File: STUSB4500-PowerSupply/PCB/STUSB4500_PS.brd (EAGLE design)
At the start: 60 x 40 mm, 102 parts, among them J2 FEMALE 2x3, J3 FEMALE 2x3, J4 FEMALE 2x3, SW1 SPST_TACT-EVQQ2

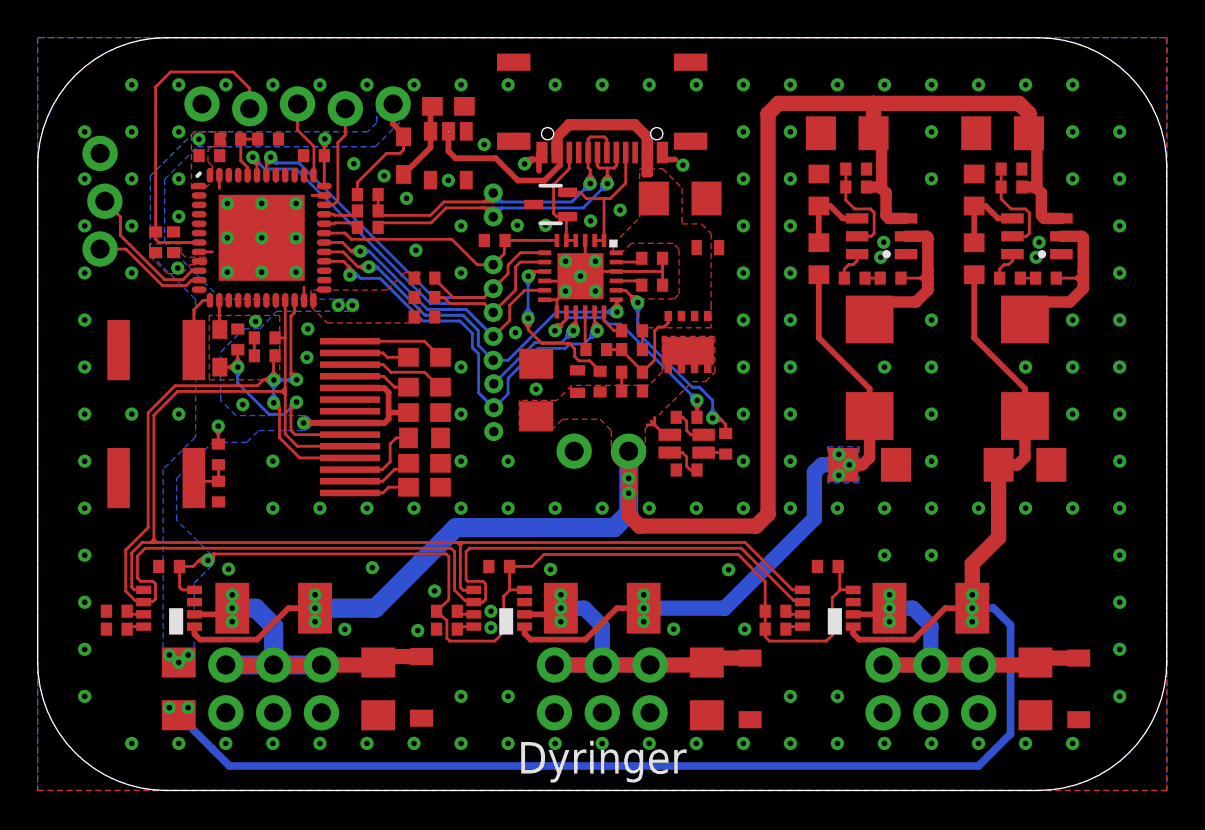
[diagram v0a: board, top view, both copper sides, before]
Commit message: removed some unnecessary elements, added uc controlled dc-dc enable
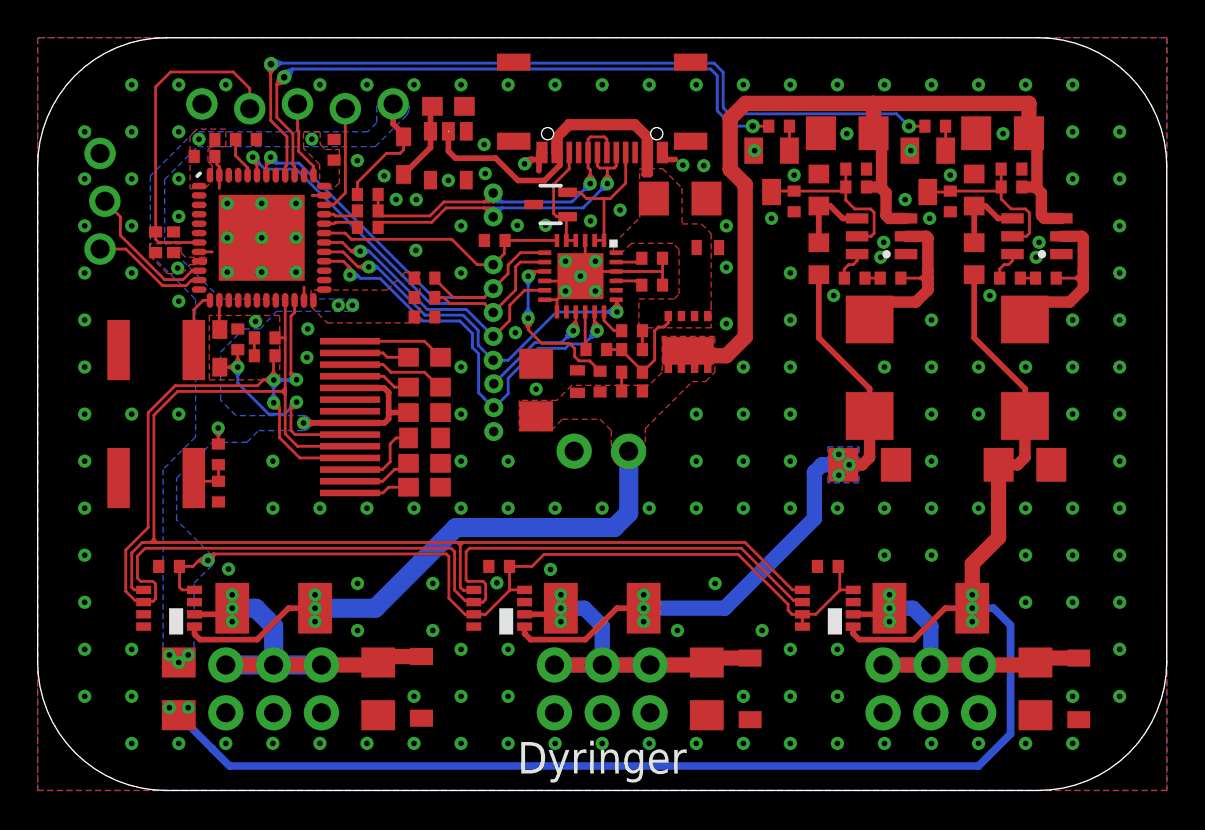
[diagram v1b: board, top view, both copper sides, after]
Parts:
- removed LED2: GM1WA55311A, led:GM1WA55311A
- removed R13, R17, R18, R20, R21, R9: 1k, DD_rcl:R0402
- removed R46, R47, R48: 22k, DD_rcl:R0402
- added C2, C3: 100nF 25V, DD_rcl:C0402
- added R2, R3: (no value), DD_rcl:R0402
- added T1, T2: BC847, transistor:SOT23
- moved R39 1.18 mm to (11.1, 34.6)
- moved C16 1.11 mm to (15.8, 34.0), turned to 90 degrees
- moved R40 0.27 mm to (9.97, 34.6)
- moved C15 0.26 mm to (8.87, 33.7)
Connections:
- removed net N$1: R17.1, U$9.8
- removed net N$13: R20.2, U$10.8
- removed net N$15: R21.2, U$10.7
- removed net N$4: R18.1, U$9.7
- removed net N$46: LED2.1, R46.2
- removed net N$47: LED2.2, R47.2
- removed net N$48: LED2.3, R48.2
- removed net N$8: R9.2, U$7.8
- removed net N$9: R13.1, U$7.7
- removed net STUSB_PDO2: R47.1, U$3.20
- removed net STUSB_PDO3: R48.1, U$3.14
- new net DC-DC-EN-3V3: R2.2, U$8.40
- new net DC-DC-EN-5V0: R3.2, U$8.39
- new net N$3: R2.1, T1.1
- new net N$5: R3.1, T2.1
- net +3V3: now also U$7.7, U$9.7, U$9.8; no longer R13.2, R17.2, R18.2
- net GND: now also C2.1, C3.1, T1.2, T2.2, U$10.7, U$10.8, U$7.8; no longer R20.1, R21.1, R46.1, R9.1
- net N$19: now also C2.2, T2.3
- net N$25: now also C3.2, T1.3
- net USB_PD_VDD: no longer LED2.4
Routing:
- net DC-DC-EN-3V3: track 0.00 -> 46.6 mm, vias 0 -> 2
- net DC-DC-EN-5V0: track 0.00 -> 37.3 mm, vias 0 -> 2
- net STUSB_PDO2: track 33.7 -> 0.00 mm, vias 2 -> 0
- net STUSB_PDO3: track 28.8 -> 0.00 mm, vias 2 -> 0
- net USB_PD_VDD: track 131.3 -> 110.7 mm, vias 5 -> 3
- net +3V3: track 88.4 -> 75.5 mm
- net N$19: track 5.50 -> 9.56 mm
- net N$25: track 5.45 -> 9.44 mm
- net N$48: track 2.13 -> 0.00 mm
- net N$46: track 2.13 -> 0.00 mm
- net N$5: track 0.00 -> 1.30 mm
- net N$3: track 0.00 -> 1.30 mm
- net N$47: track 1.25 -> 0.00 mm
- net GND: track 26.3 -> 27.4 mm, vias 183 -> 205
- net N$4: track 0.96 -> 0.00 mm
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
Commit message: Fixed OLED design, moved some lines
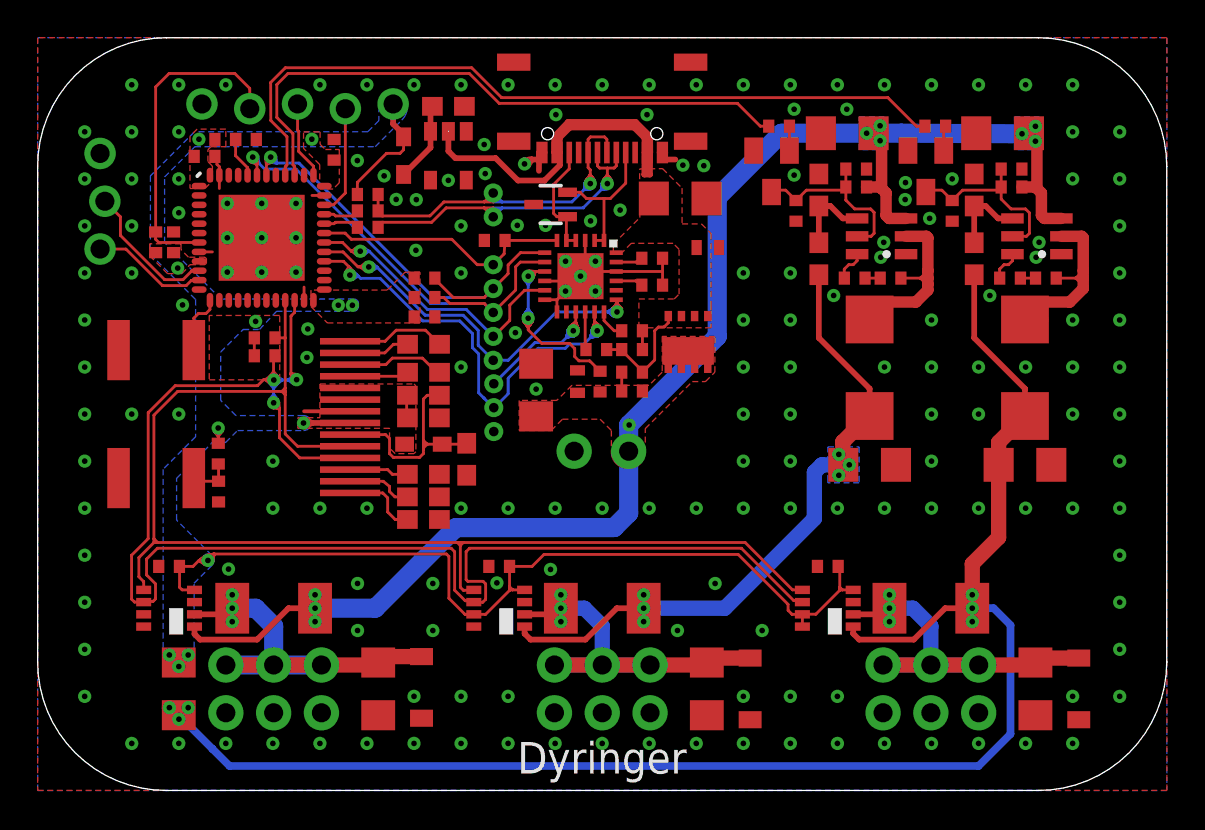
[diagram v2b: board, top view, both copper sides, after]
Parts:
- added C4: 10uF 6.3V, DD_rcl:C0603
- R31: device DD_rcl:R0402 -> DD_rcl:R0603
- moved D2 12.0 mm to (20.5, 18.4), turned to 180 degrees
- moved R31 10.3 mm to (20.5, 21.0), turned to 180 degrees
- moved R30 1.93 mm to (20.5, 16.8)
- moved C21 1.78 mm to (20.5, 15.6)
- moved C20 1.71 mm to (20.5, 14.4)
- moved C23 0.79 mm to (20.5, 22.2)
- moved C24 0.69 mm to (20.5, 23.7)
- moved C3 0.51 mm to (48.6, 30.8)
- moved C2 0.51 mm to (40.3, 30.8)
- moved C22 0.29 mm to (20.5, 19.8)
- moved T1 0.10 mm to (47.2, 32.9)
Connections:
- removed net OLED_RST*: D2.C, U$8.14
- net +3V3: now also D2.C
- net GND: now also C4.1
- net OLED_RST: now also C4.2
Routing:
- net OLED_RST: track 18.0 -> 11.7 mm, vias 2 -> 0
- net +3V3: track 75.5 -> 70.1 mm
- net DC-DC-EN-3V3: track 46.6 -> 41.7 mm, vias 2 -> 0
- net DC-DC-EN-5V0: track 37.3 -> 32.8 mm, vias 2 -> 0
- net GND: track 27.4 -> 29.8 mm, vias 205 -> 186
- net USB_PD_VDD: track 110.7 -> 109.0 mm, vias 3 -> 10
- net OLED_RST*: track 1.56 -> 0.00 mm
- net SDA_2: track 91.2 -> 89.8 mm
- net SCL_2: track 69.9 -> 68.5 mm
- net N$40: track 4.36 -> 3.15 mm
- net N$41: track 3.23 -> 4.07 mm
- net DC-DC-3V3: track 101.0 -> 100.4 mm, vias 5 -> 6
- net N$25: track 9.44 -> 10.00 mm

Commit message: Changed DC-DC coils to Wurth
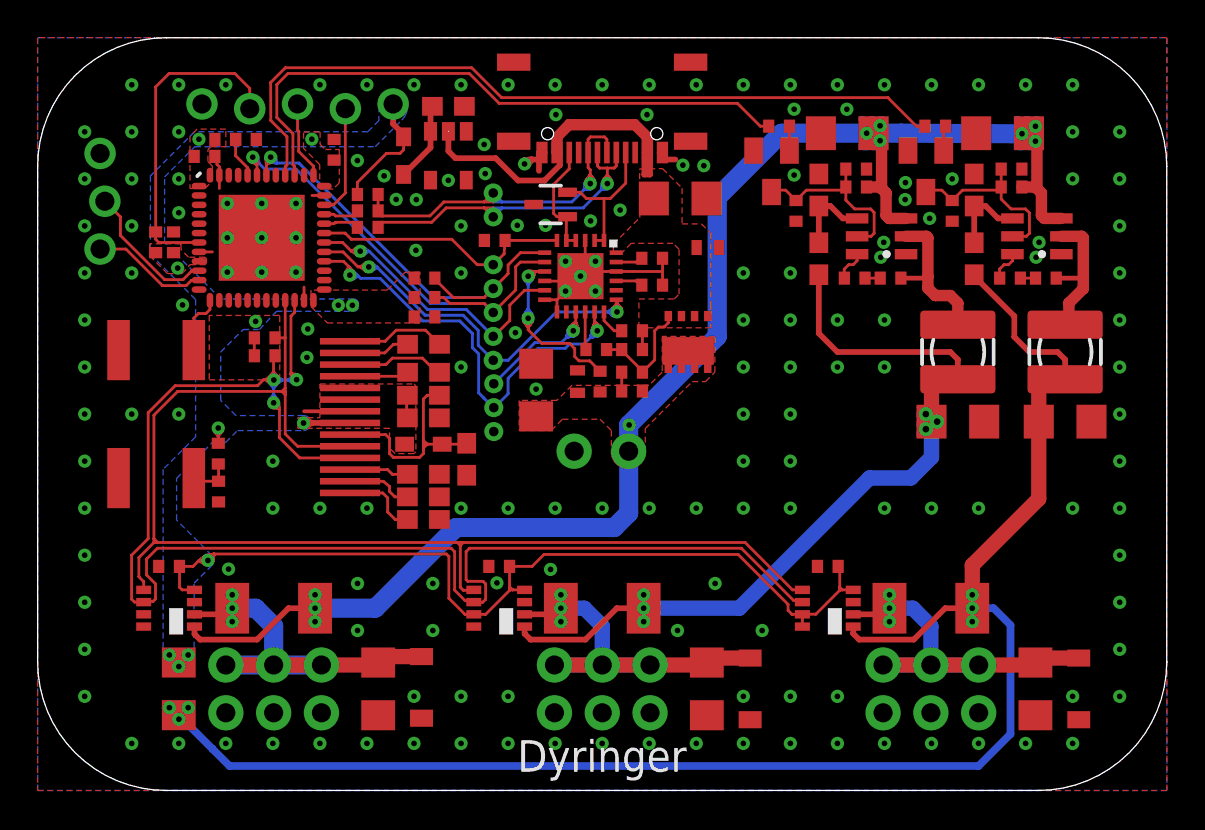
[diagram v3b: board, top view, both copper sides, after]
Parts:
- L1, L2: device DD_rcl:PIS2816 -> DD_rcl:POWER-CHOKE_WE-TPC
- moved C10 5.22 mm to (48.9, 19.6)
- moved L1 4.76 mm to (48.9, 23.3)
- moved C13 3.13 mm to (54.6, 19.6)
- moved L2 2.29 mm to (54.6, 23.3)
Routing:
- net DC-DC-5V0: track 70.3 -> 78.8 mm
- net DC-DC-3V3: track 100.4 -> 104.0 mm
- net N$30: track 11.4 -> 7.81 mm
- net N$26: track 10.2 -> 8.41 mm
- net GND: vias 186 -> 175
